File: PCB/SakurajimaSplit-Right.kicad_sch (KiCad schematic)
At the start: 0 parts

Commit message: feat(sch): design right half of the keyboard
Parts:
- added C12, C16, C17, C18, C19: 100nF, symbol Device:C
- added C13, C14: 20pF, symbol Device:C
- added C15: 4.7uF, symbol Device:C
- added D25: CapsLock ind., symbol Device:LED
- added H5, H6, H7, H8: MountingHole, symbol Mechanical:MountingHole
- added J19, J22, J23, J25, J26, J27, J28, J29, J30, J31, J32, J33, J34, J35, J36, J37, J39: Conn_01x01_Pin, symbol Connector:Conn_01x01_Pin
- added J20: SWD, symbol Connector_Generic:Conn_01x05
- added J24: Conn_01x01_Pin, Connector_Wire:SolderWirePad_1x01_SMD_1x2mm, symbol Connector:Conn_01x01_Pin
- added R12: 330R, symbol Device:R_Small
- added R13: TBD, symbol Device:R
- added R14, R15, R16, R17, R18, R19: 10k, symbol Device:R_Small
- added SW3: SWCLK/BOOT0, symbol Switch:SW_Push
- added SW4: Knob, symbol Device:RotaryEncoder_Switch
- added TP16, TP17, TP18, TP19: GND, symbol Connector:TestPoint
- added TP20: Display_SCLK, symbol Connector:TestPoint
- added TP21: Display_SDI, symbol Connector:TestPoint
- added U7: STM32G0B1CBT6, Package_QFP:LQFP-48_7x7mm_P0.5mm, symbol MCU_ST_STM32G0:STM32G0B1CBTx
- added U8: ZJY_M233, Hayata_Lib:OLED_SSD1305, symbol Hayata_Lib:OLED_SSD1305
- added Y2: 8MHz, symbol Device:Crystal_GND24
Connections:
- new net: J28.1 (Pin_1), U7.18 (PA7)
- new net: C14.1, R13.1, Y2.3
- new net: R15.1, R18.2, SW4.B
- new net: J27.1 (Pin_1), U7.17 (PA6)
- new net: J39.1 (Pin_1), U7.34 (PA10/PA12)
- new net: J32.1 (Pin_1), U7.31 (PC7)
- new net: J25.1 (Pin_1), U7.15 (PA4)
- new net: J31.1 (Pin_1), U7.30 (PC6)
- new net: R14.1, R17.2, SW4.A
- new net: R16.1, R19.2, SW4.S1
- new net: J36.1 (Pin_1), U7.42 (PB3)
- new net: J30.1 (Pin_1), U7.29 (PA9/UCPD1_DBCC1)
- new net: J19.1 (Pin_1), U7.33 (PA9/PA11)
- new net: J24.1 (Pin_1), U7.12 (PA1)
- new net: J29.1 (Pin_1), U7.28 (PA8)
- new net: J26.1 (Pin_1), U7.16 (PA5)
- new net: J34.1 (Pin_1), U7.37 (PA15)
- new net: D25.1 (K), R12.1
- new net: J22.1 (Pin_1), U7.5 (VREF+)
- new net: J33.1 (Pin_1), U7.32 (PA10/UCPD1_DBCC2)
- new net: J35.1 (Pin_1), U7.19 (PB0)
- new net: J23.1 (Pin_1), U7.11 (PA0)
- new net: J37.1 (Pin_1), U7.26 (PB14)
- new net +3.3V: C12.1, C15.1, C16.1, J20.1 (Pin_1), R14.2, R15.2, R16.2, SW3.2, U7.4 (VBAT), U7.6 (VDD), U8.2 (3.3V)
- new net COL0: U7.43 (PB4)
- new net COL1: U7.44 (PB5)
- new net COL2: U7.45 (PB6)
- new net COL3: U7.46 (PB7)
- new net COL4: U7.47 (PB8)
- new net COL5: U7.48 (PB9)
- new net CapsLock: D25.2 (A), U7.20 (PB1)
- new net Display_DC: U7.21 (PB2), U8.6 (DC)
- new net Display_SCLK: TP20.1, U7.25 (PB13), U8.3 (SCL/SCLK)
- new net Display_SDI: TP21.1, U7.27 (PB15), U8.4 (SDA/SDIN)
- new net Display_~{CS}: U7.23 (PB11), U8.7 (~{CS})
- new net Display_~{EN}: U7.24 (PB12), U8.8 (~{EN})
- new net Display_~{RST}: U7.22 (PB10), U8.5 (~{RST})
- new net GND: C13.2, C14.2, C15.2, C16.2, C17.2, C18.2, C19.2, J20.5 (Pin_5), R12.2, SW4.C, SW4.S2, TP16.1, TP17.1, TP18.1, TP19.1, U7.7 (VSS), U8.1 (GND), Y2.2, Y2.4
- new net HSE_IN: C13.1, U7.8 (PF0), Y2.1
- new net HSE_OUT: R13.2, U7.9 (PF1)
- new net Knob_A: C17.1, R17.1, U7.1 (PC13)
- new net Knob_B: C18.1, R18.1, U7.2 (PC14)
- new net Knob_SW: C19.1, R19.1, U7.3 (PC15)
- new net NRST: J20.4 (Pin_4), U7.10 (PF2)
- new net ROW0: U7.38 (PD0)
- new net ROW1: U7.39 (PD1)
- new net ROW2: U7.40 (PD2)
- new net ROW3: U7.41 (PD3)
- new net SWCLK/BOOT0: C12.2, J20.3 (Pin_3), SW3.1, U7.36 (PA14)
- new net SWDIO: J20.2 (Pin_2), U7.35 (PA13)
- new net USART_RX: U7.14 (PA3)
- new net USART_TX: U7.13 (PA2)
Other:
- added sheet Key-Matrix (SakurajimaSplit-Right-Matrix.kicad_sch)
- added sheet Power (SakurajimaSplit-Right-Power.kicad_sch)
- note added: "BOOT0 Switch"
- note added: "CapsLock ind."
- note added: "GND Test points"
- note added: "HSE (8MHz)"
- note added: "OLED Display"
- note added: "Rotary Encoder"
- note added: "Serial Wire Debug"

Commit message: fix(sch): fix ERC errors regarding power flags
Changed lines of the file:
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@@
 	)
 	(junction
-		(at 44.45 52.07)
-		(diameter 0)
-		(color 0 0 0 0)
-	)
-	(junction
 		(at 85.09 138.43)
 		(diameter 0)
@@
 					(unit 1)
 				)
-			)
-		)
-	)
-	(symbol
-		(lib_id "power:PWR_FLAG")
-		(at 44.45 52.07 270)
-		(unit 1)
-		(exclude_from_sim no)
-		(in_bom yes)
-		(on_board yes)
-		(dnp no)
-		(fields_autoplaced yes)
-		(property "Reference" "#FLG05"
-			(at 46.355 52.07 0)
-			(effects
-				(font
-					(size 1.27 1.27)
-				)
-				(hide yes)
-			)
-		)
-		(property "Value" "PWR_FLAG"
-			(at 49.53 52.07 0)
-			(effects
-				(font
-					(size 1.27 1.27)
-				)
-				(hide yes)
-			)
-		)
-		(property "Footprint" ""
-			(at 44.45 52.07 0)
-			(effects
-				(font
-					(size 1.27 1.27)
-					(thickness 0.254)
-					(bold yes)
-				)
-				(hide yes)
-			)
-		)
-		(property "Datasheet" "~"
-			(at 44.45 52.07 0)
-			(effects
-				(font
-					(size 1.27 1.27)
-					(thickness 0.254)
-					(bold yes)
-				)
-				(hide yes)
-			)
-		)
-		(property "Description" "Special symbol for telling ERC where power comes from"
-			(at 44.45 52.07 0)
-			(effects
-				(font
-					(size 1.27 1.27)
-					(thickness 0.254)
-					(bold yes)
-				)
-				(hide yes)
-			)
-		)
-		(pin "1"
-		)
-		(instances
-			(project "SakurajimaSplit"
-				(path "/2049b6de-7453-46e1-ab60-70116abff9d6/2fb40ee0-3e4b-4e2d-8d4c-b78786a3c10e"
-					(reference "#FLG05")
-					(unit 1)
-				)

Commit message: feat(pcb): assign all footprints
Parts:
- C12, C16, C17, C18, C19: footprint (none) -> Capacitor_SMD:C_0603_1608Metric
- C13, C14: footprint (none) -> Capacitor_SMD:C_0402_1005Metric_Pad0.74x0.62mm_HandSolder
- C15: footprint (none) -> Capacitor_SMD:C_0805_2012Metric
- D25: footprint (none) -> LED_SMD:LED_0603_1608Metric
- H5, H6, H7, H8: footprint (none) -> MountingHole:MountingHole_3.2mm_M3_Pad
- J20: footprint (none) -> Connector_PinHeader_2.54mm:PinHeader_1x05_P2.54mm_Horizontal
- J21: renamed from J22; footprint (none) -> Connector_Wire:SolderWirePad_1x01_SMD_1x2mm
- J22: renamed from J23; footprint (none) -> Connector_Wire:SolderWirePad_1x01_SMD_1x2mm
- J24: renamed from J25; footprint (none) -> Connector_Wire:SolderWirePad_1x01_SMD_1x2mm
- J25: renamed from J26; footprint (none) -> Connector_Wire:SolderWirePad_1x01_SMD_1x2mm
- J26: renamed from J27; footprint (none) -> Connector_Wire:SolderWirePad_1x01_SMD_1x2mm
- J27: renamed from J28; footprint (none) -> Connector_Wire:SolderWirePad_1x01_SMD_1x2mm
- J28: renamed from J29; footprint (none) -> Connector_Wire:SolderWirePad_1x01_SMD_1x2mm
- J29: renamed from J19; footprint (none) -> Connector_Wire:SolderWirePad_1x01_SMD_1x2mm
- J30, J31: footprint (none) -> Connector_Wire:SolderWirePad_1x01_SMD_1x2mm
- J32: renamed from J39; footprint (none) -> Connector_Wire:SolderWirePad_1x01_SMD_1x2mm
- J33: renamed from J32; footprint (none) -> Connector_Wire:SolderWirePad_1x01_SMD_1x2mm
- J34: renamed from J33; footprint (none) -> Connector_Wire:SolderWirePad_1x01_SMD_1x2mm
- J35: renamed from J34; footprint (none) -> Connector_Wire:SolderWirePad_1x01_SMD_1x2mm
- J36: renamed from J35; footprint (none) -> Connector_Wire:SolderWirePad_1x01_SMD_1x2mm
- J37: renamed from J36; footprint (none) -> Connector_Wire:SolderWirePad_1x01_SMD_1x2mm
- J38: renamed from J37; footprint (none) -> Connector_Wire:SolderWirePad_1x01_SMD_1x2mm
- R12, R13, R14, R15, R16, R17, R18, R19: footprint (none) -> Resistor_SMD:R_0603_1608Metric
- SW3: footprint (none) -> Button_Switch_SMD:SW_Push_1P1T_XKB_TS-1187A
- SW4: footprint (none) -> Rotary_Encoder:RotaryEncoder_Alps_EC11E-Switch_Vertical_H20mm
- TP14: renamed from TP16; footprint (none) -> TestPoint:TestPoint_Pad_2.0x2.0mm
- TP15: renamed from TP17; footprint (none) -> TestPoint:TestPoint_Pad_2.0x2.0mm
- TP16: renamed from TP18; footprint (none) -> TestPoint:TestPoint_Pad_2.0x2.0mm
- TP17: renamed from TP19; footprint (none) -> TestPoint:TestPoint_Pad_2.0x2.0mm
- TP18: renamed from TP20; footprint (none) -> TestPoint:TestPoint_Pad_2.0x2.0mm
- TP19: renamed from TP21; footprint (none) -> TestPoint:TestPoint_Pad_2.0x2.0mm
- Y2: footprint (none) -> Crystal:Crystal_SMD_3225-4Pin_3.2x2.5mm_HandSoldering
- renumbered J24 to J23, U7 to U6, U8 to U7

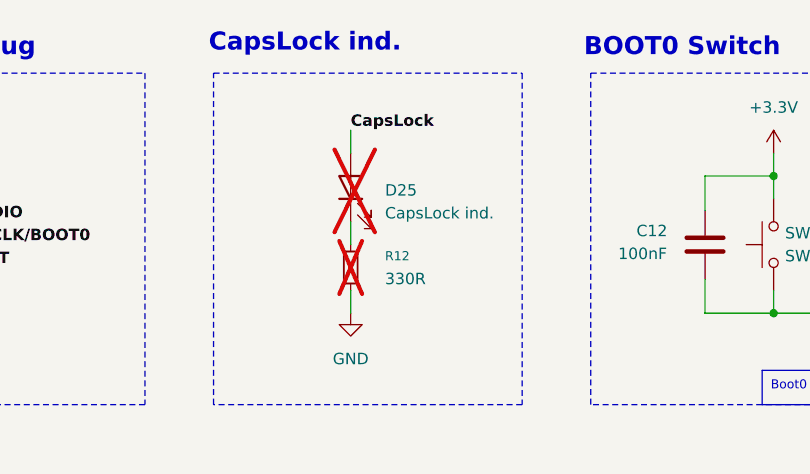
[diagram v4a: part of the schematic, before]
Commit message: fix(sch): fix matrix diode designators not starting from 1
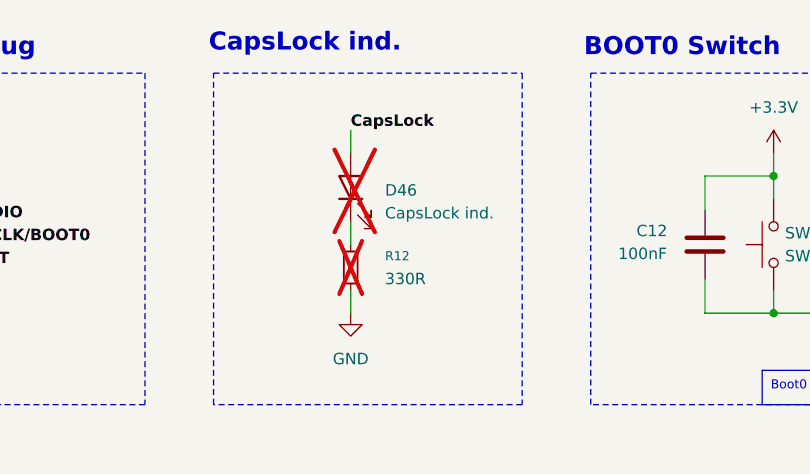
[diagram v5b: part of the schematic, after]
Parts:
- renumbered D25 to D46
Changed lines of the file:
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@@
 		(dnp yes)
 		(fields_autoplaced yes)
-		(property "Reference" "D25"
+		(property "Reference" "D46"
 			(at 91.44 40.9574 90)
 			(effects
@@
 			(project "SakurajimaSplit"
 				(path "/2049b6de-7453-46e1-ab60-70116abff9d6/2fb40ee0-3e4b-4e2d-8d4c-b78786a3c10e"
-					(reference "D25")
+					(reference "D46")
 					(unit 1)
 				)

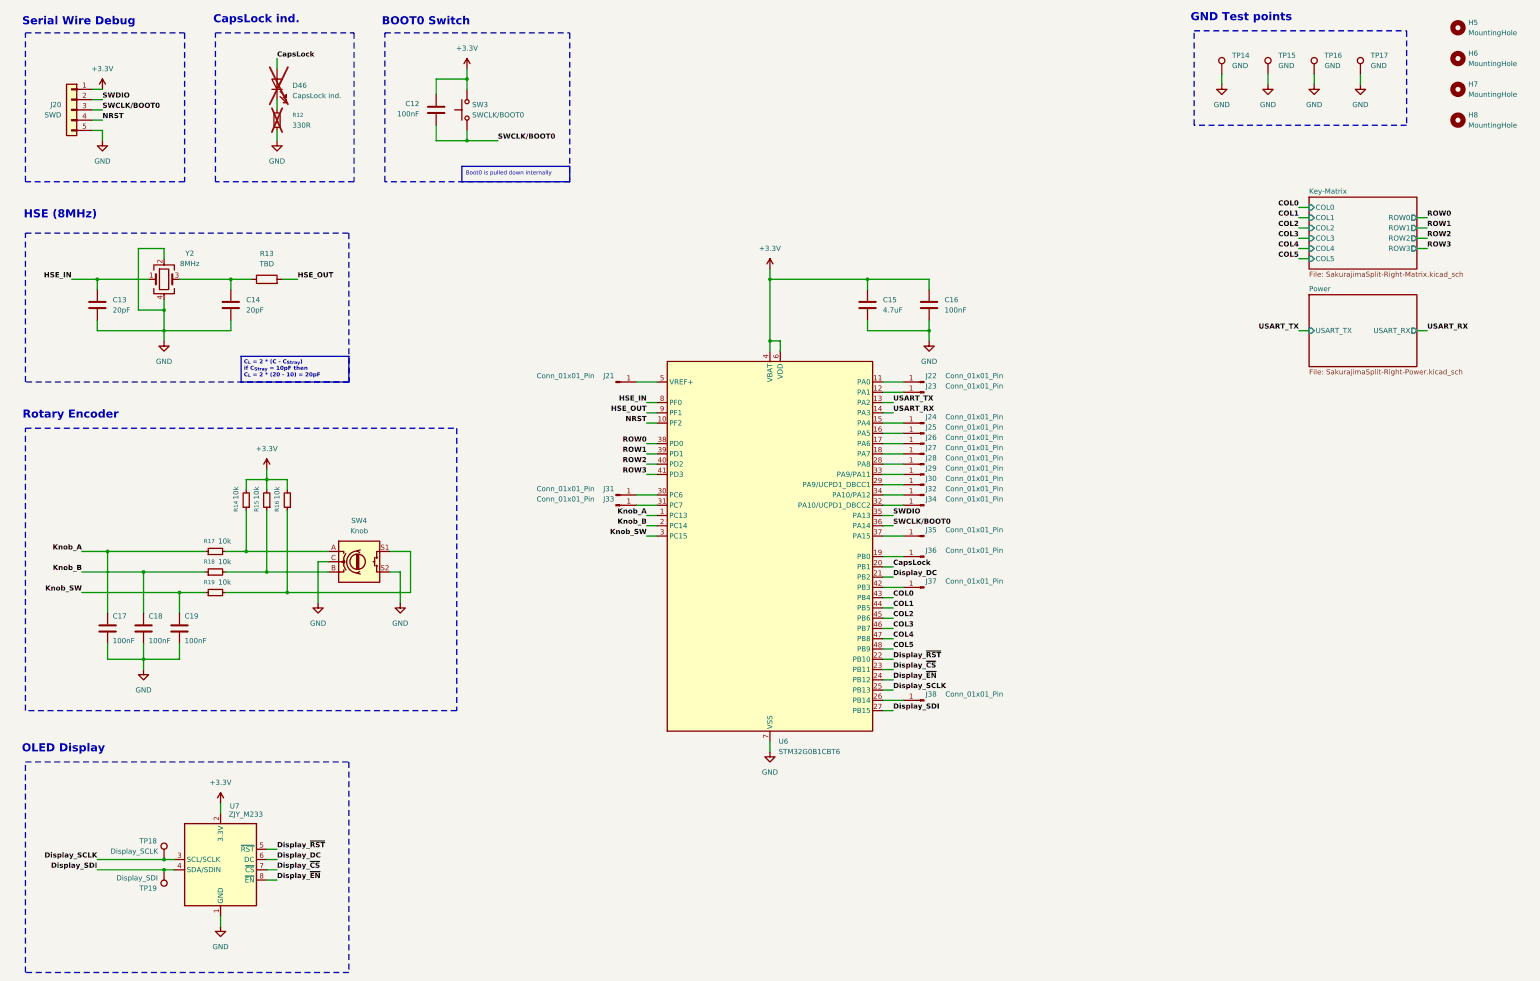
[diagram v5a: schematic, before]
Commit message: feat(sch): add spi flash, remove rotary encoder, fix footprints
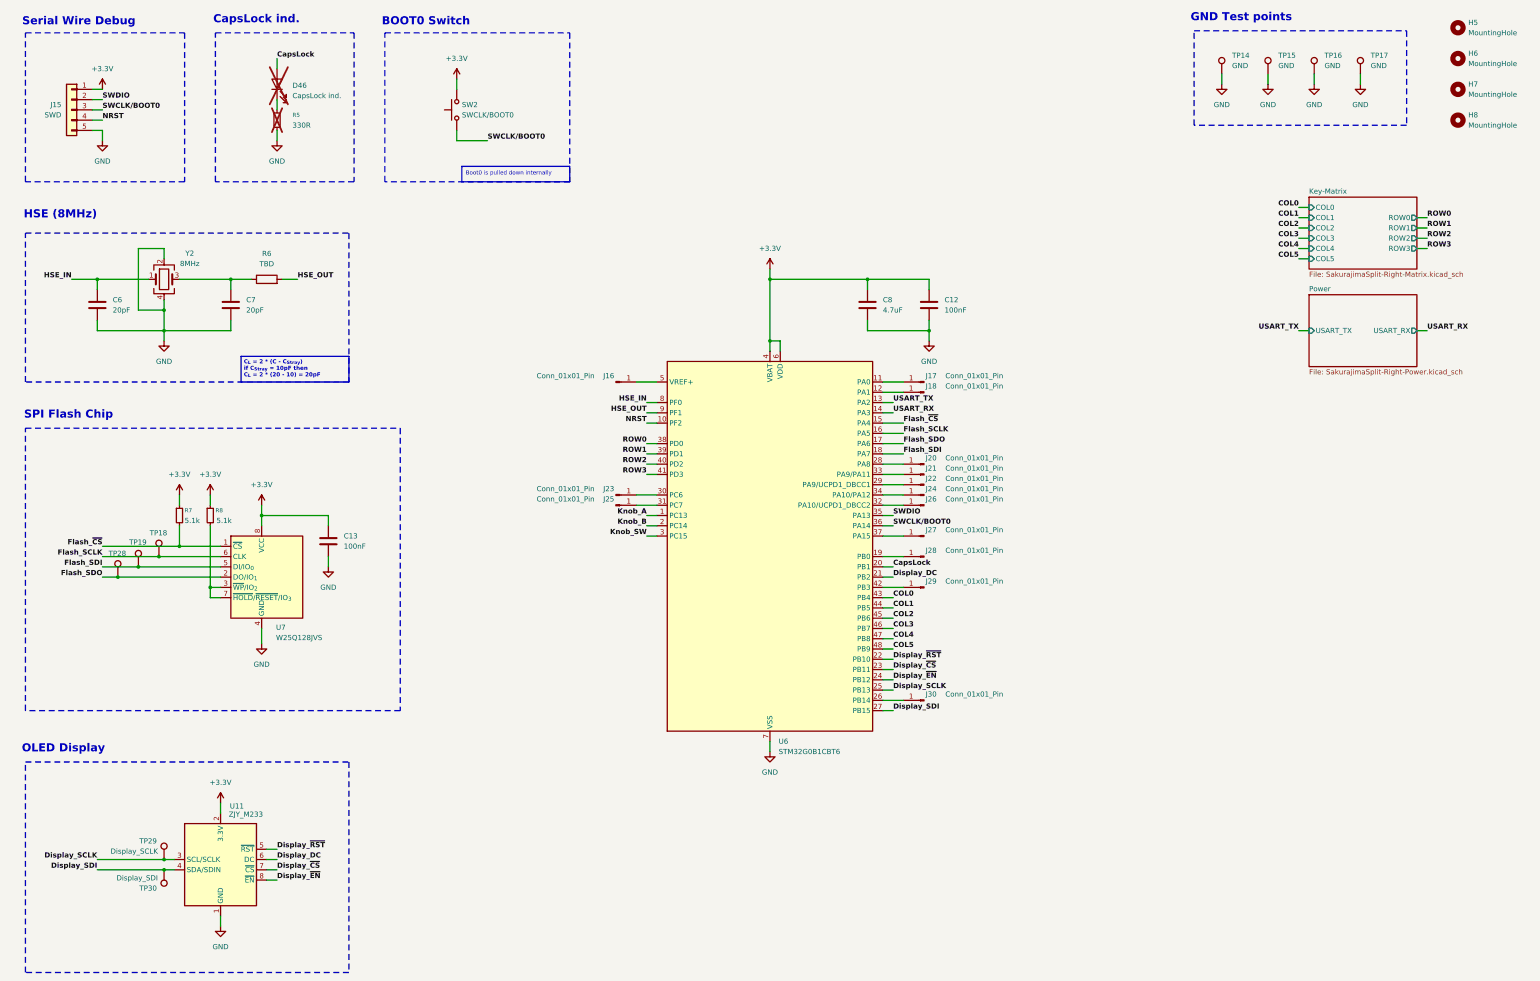
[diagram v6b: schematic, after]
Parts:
- removed C12, C17, C18, C19: 100nF, Capacitor_SMD:C_0603_1608Metric, symbol Device:C
- removed J24, J25, J26, J27: Conn_01x01_Pin, Connector_Wire:SolderWirePad_1x01_SMD_1x2mm, symbol Connector:Conn_01x01_Pin
- removed R14, R15, R16, R17, R18, R19: 10k, Resistor_SMD:R_0603_1608Metric, symbol Device:R_Small
- removed SW4: Knob, Rotary_Encoder:RotaryEncoder_Alps_EC11E-Switch_Vertical_H20mm, symbol Device:RotaryEncoder_Switch
- added C13: 100nF, Capacitor_SMD:C_0603_1608Metric, symbol Device:C
- added R7, R8: 5.1k, Resistor_SMD:R_0603_1608Metric, symbol Device:R_Small
- added TP18: Flash_SCLK, Hayata_Lib:TestPoint_Pad_Circular_1.3mm, symbol Connector:TestPoint
- added TP19: Flash_SDI, Hayata_Lib:TestPoint_Pad_Circular_1.3mm, symbol Connector:TestPoint
- added TP28: Flash_SDO, Hayata_Lib:TestPoint_Pad_Circular_1.3mm, symbol Connector:TestPoint
- added U7: W25Q128JVS, Package_SO:SOIC-8_5.3x5.3mm_P1.27mm, symbol Memory_Flash:W25Q128JVS
- SW2: renamed from SW3; footprint Button_Switch_SMD:SW_Push_1P1T_XKB_TS-1187A -> Hayata_Lib:SW_Push_TS-1010B
- TP14, TP15, TP16, TP17: footprint TestPoint:TestPoint_Pad_2.0x2.0mm -> Hayata_Lib:TestPoint_Pad_Circular_1.3mm
- TP29: renamed from TP18; footprint TestPoint:TestPoint_Pad_2.0x2.0mm -> Hayata_Lib:TestPoint_Pad_Circular_1.3mm
- TP30: renamed from TP19; footprint TestPoint:TestPoint_Pad_2.0x2.0mm -> Hayata_Lib:TestPoint_Pad_Circular_1.3mm
- Y2: footprint Crystal:Crystal_SMD_3225-4Pin_3.2x2.5mm_HandSoldering -> Crystal:Crystal_SMD_3225-4Pin_3.2x2.5mm
- renumbered C16 to C12, C13 to C6, C14 to C7, C15 to C8, J20 to J15, J21 to J16, J22 to J17, J23 to J18, J28 to J20, J29 to J21, J30 to J22, J31 to J23, J32 to J24, J33 to J25, J34 to J26, J35 to J27, J36 to J28, J37 to J29, J38 to J30, R12 to R5, R13 to R6, U7 to U11
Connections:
- net +3.3V: now also C13.1, R7.1, R8.1, U7.8 (VCC)
- net GND: now also C13.2, U7.4 (GND)
- net Flash_SDI: now reaches U6.18 (PA7)
- net Flash_SDI: now also TP19.1, U7.5 (DI/IO_{0})
- net Flash_SDO: now reaches U6.17 (PA6)
- net Flash_SDO: now also TP28.1, U7.2 (DO/IO_{1})
- net Flash_~{CS}: now reaches U6.15 (PA4)
- net Flash_~{CS}: now also R7.2, U7.1 (~{CS})
- net Flash_SCLK: now reaches U6.16 (PA5)
- net Flash_SCLK: now also TP18.1, U7.6 (CLK)
- new net: R8.2, U7.3 (~{WP}/IO_{2}), U7.7 (~{HOLD}/~{RESET}/IO_{3})
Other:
- note added: "SPI Flash Chip"
- note removed: "Rotary Encoder"
- moved on the sheet: SW2
